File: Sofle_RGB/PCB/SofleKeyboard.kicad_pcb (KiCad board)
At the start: 2 copper layers, 143.4 x 111.8 mm, 97 parts, among them J1 LED, J2 4PIN, J3 OLED, J4 key leds, J5 backlight sel, J6 indicator bypass, P1 i2c_pin, P2 i2c_pin, SW1 SW_PUSH-MX_W_LED, SW10 SW_PUSH-MX_W_LED, SW11 SW_PUSH-MX_W_LED, SW12 SW_PUSH-MX_W_LED, SW13 SW_PUSH-MX_W_LED, SW14 SW_PUSH-MX_W_LED, SW15 SW_PUSH-MX_W_LED, SW16 SW_PUSH-MX_W_LED, SW17 SW_PUSH-MX_W_LED, SW18 SW_PUSH-MX_W_LED, SW19 SW_PUSH-MX_W_LED, SW2 SW_PUSH-MX_W_LED, SW20 SW_PUSH-MX_W_LED, SW21 SW_PUSH-MX_W_LED, SW22 SW_PUSH-MX_W_LED, SW23 SW_PUSH-MX_W_LED, SW24 SW_PUSH-MX_W_LED, SW25 Rotary_Encoder_Switch, SW26 SW_PUSH-MX_W_LED, SW27 SW_PUSH-MX_W_LED, SW28 SW_PUSH-MX_W_LED, SW29 SW_PUSH-MX_W_LED, SW3 SW_PUSH-MX_W_LED, SW30 SW_PUSH-MX_W_LED, SW4 SW_PUSH-MX_W_LED, SW5 SW_PUSH-MX_W_LED, SW6 SW_PUSH-MX_W_LED, SW7 SW_PUSH-MX_W_LED, SW8 SW_PUSH-MX_W_LED, SW9 SW_PUSH-MX_W_LED, U1 ProMicro

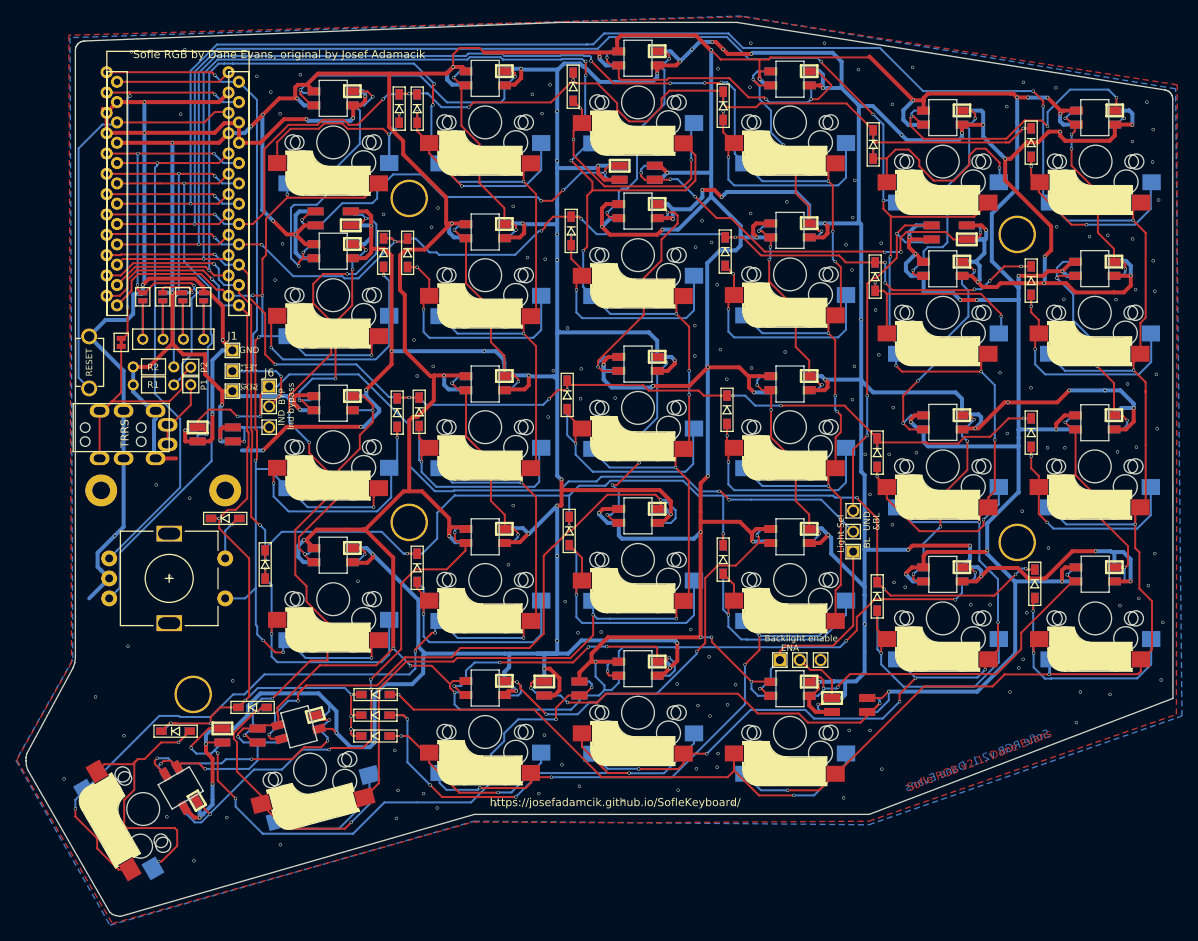
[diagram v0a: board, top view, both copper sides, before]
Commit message: First pass at comparison graphics Revised all keyboards to use outline stubbs Generated nested SVG's and color pallete
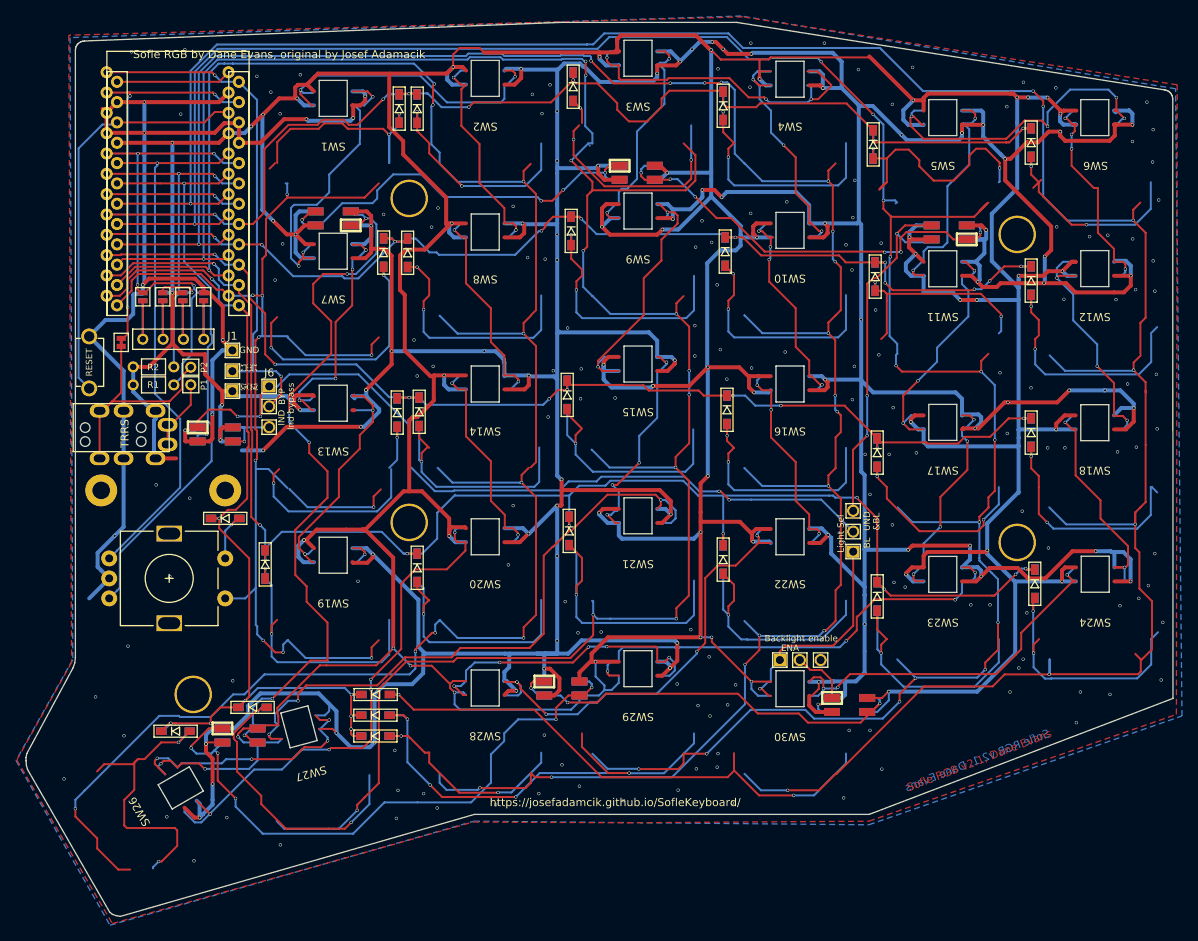
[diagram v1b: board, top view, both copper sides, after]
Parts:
- SW1, SW10, SW11, SW12, SW13, SW14, SW15, SW16, SW17, SW18, SW19, SW2, SW20, SW21, SW22, SW23, SW24, SW26, SW27, SW28, SW29, SW3, SW30, SW4, SW5, SW6, SW7, SW8, SW9: footprint Button_Switch_Keyboard:SK6812MINI_and_cherry -> ergodonk_kicad_library:key_outline_only
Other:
- net class Default removed
- net class GND removed
- net class VCC removed
